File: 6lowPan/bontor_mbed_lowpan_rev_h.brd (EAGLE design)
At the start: 99.6 x 107 mm, 173 parts, among them IC1 SIM900, IC2 74HC595D, IC3 74HC595D, IC4 ADE7758RW, IC5 74HC595D, U2 W5500, X1 NX2520SA

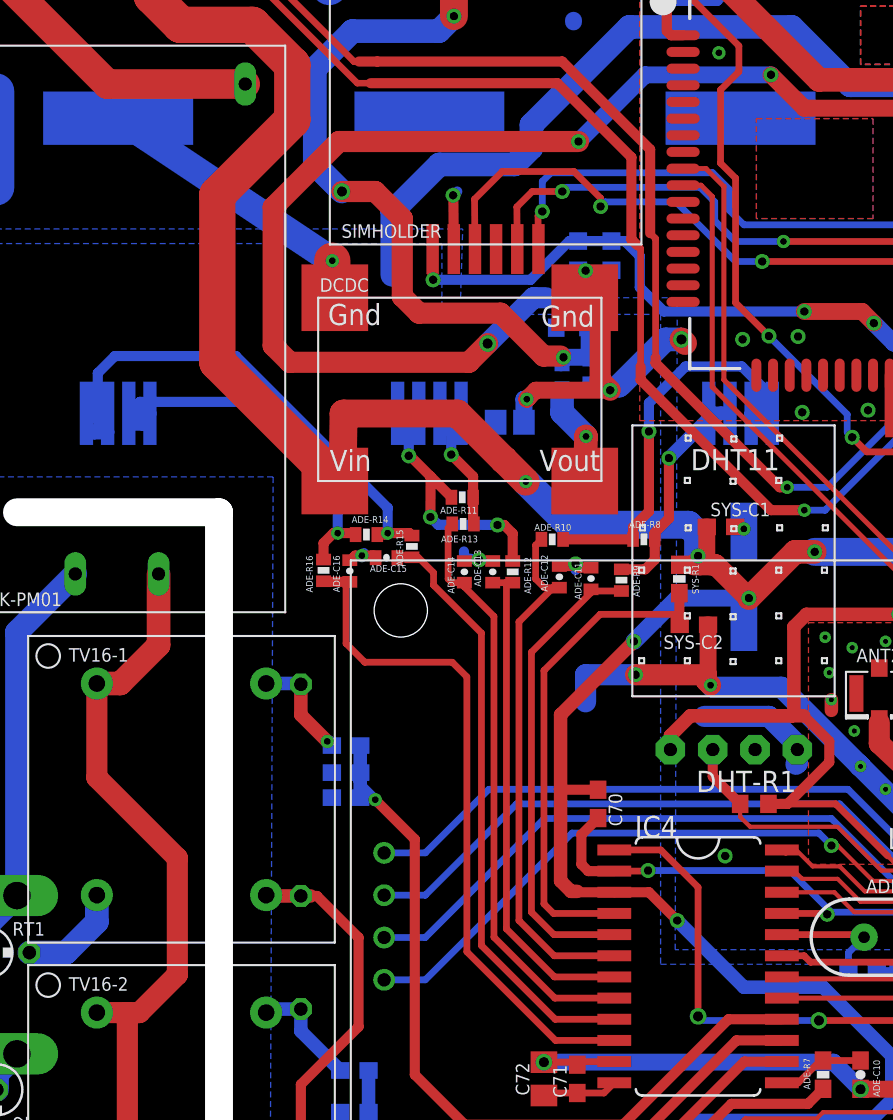
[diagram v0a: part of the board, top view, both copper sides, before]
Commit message: add mcb enhancer BoM and gerber
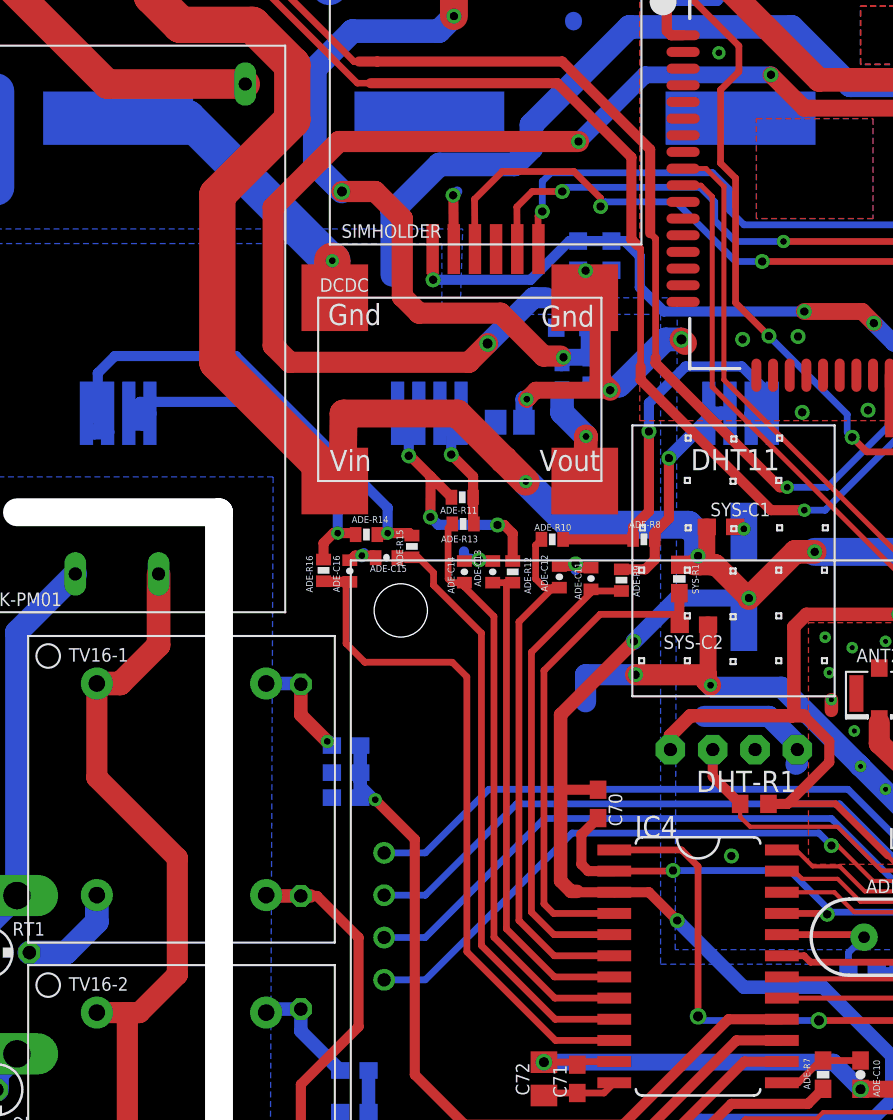
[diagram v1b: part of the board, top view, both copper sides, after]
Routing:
- net DGND: track 380.0 -> 381.0 mm
- net ADE_APCF: track 46.3 -> 47.0 mm
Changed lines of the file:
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@@
 <setting verticaltext="up"/>
 </settings>
-<grid distance="1" unitdist="mm" unit="mm" style="lines" multiple="1" display="yes" altdistance="0.125" altunitdist="mm" altunit="mm"/>
+<grid distance="0.125" unitdist="mm" unit="mm" style="lines" multiple="1" display="yes" altdistance="0.125" altunitdist="mm" altunit="mm"/>
 <layers>
 <layer number="1" name="Top" color="4" fill="1" visible="yes" active="yes"/>
@@
 <wire x1="87.25" y1="36.25" x2="87.25" y2="36.275" width="0.254" layer="1"/>
 <via x="76.25" y="63" extent="1-16" drill="0.6" shape="octagon"/>
-<via x="40.75" y="42.75" extent="1-16" drill="0.5" shape="octagon"/>
-<wire x1="40.75" y1="42.75" x2="49.25" y2="42.75" width="0.4064" layer="16"/>
+<via x="42.25" y="42.75" extent="1-16" drill="0.5" shape="octagon"/>
+<wire x1="42.25" y1="42.75" x2="49.25" y2="42.75" width="0.4064" layer="16"/>
 <wire x1="49.25" y1="42.75" x2="51.75" y2="40.25" width="0.4064" layer="16"/>
 <wire x1="51.75" y1="40.25" x2="55.75" y2="40.25" width="0.4064" layer="16"/>
 <wire x1="55.75" y1="40.25" x2="56.25" y2="39.75" width="0.4064" layer="16"/>
 <wire x1="56.25" y1="39.75" x2="56.25" y2="36.875" width="0.4064" layer="16"/>
-<wire x1="38.7208" y1="42.715" x2="40.715" y2="42.715" width="0.4064" layer="1"/>
-<wire x1="40.715" y1="42.715" x2="40.75" y2="42.75" width="0.4064" layer="1"/>
+<wire x1="38.7208" y1="42.715" x2="42.215" y2="42.715" width="0.4064" layer="1"/>
 <contactref element="SR_OUT1" pad="2"/>
 <contactref element="SR_OUT2" pad="2"/>
@@
 <wire x1="73.7" y1="101.25" x2="72.875" y2="101.3" width="1.4224" layer="1"/>
 <wire x1="72.875" y1="101.3" x2="73" y2="101.375" width="1.4224" layer="1"/>
-<via x="45.375" y="43.625" extent="1-16" drill="0.5"/>
+<via x="45.75" y="43.625" extent="1-16" drill="0.5"/>
 <wire x1="86.25" y1="36.625" x2="86.6" y2="36.275" width="0.254" layer="1"/>
 <wire x1="86.6" y1="36.275" x2="87.25" y2="36.275" width="0.254" layer="1"/>
@@
 <wire x1="10.45" y1="103.45" x2="10.45" y2="105.75" width="0.4064" layer="1"/>
 <wire x1="10.45" y1="105.75" x2="10.4" y2="105.75" width="0.4064" layer="1"/>
-<wire x1="8.95" y1="87.9" x2="21.8" y2="79.345" width="1.6764" layer="16"/>
 <wire x1="19.485" y1="105.75" x2="20.76" y2="104.075" width="1.27" layer="1"/>
 <via x="29.05" y="83.275" extent="1-16" drill="0.5"/>
@@
 <wire x1="10.45" y1="105.75" x2="10.85" y2="106.15" width="1.4" layer="1"/>
 <wire x1="10.85" y1="106.15" x2="11.75" y2="106.15" width="1.4" layer="1"/>
+<wire x1="21.8" y1="79.345" x2="21.655" y2="79.345" width="2.1844" layer="16"/>
+<wire x1="21.655" y1="79.345" x2="13.1" y2="87.9" width="2.1844" layer="16"/>
+<wire x1="13.1" y1="87.9" x2="8.95" y2="87.9" width="2.1844" layer="16"/>
+<wire x1="42.215" y1="42.715" x2="42.25" y2="42.75" width="0.4064" layer="1"/>
 </signal>
 <signal name="VDD">
@@
 <wire x1="48.7942" y1="44" x2="48.7792" y2="43.985" width="0.254" layer="1"/>
 <wire x1="48.8892" y1="43.875" x2="48.7792" y2="43.985" width="0.254" layer="1"/>
-<wire x1="49.0142" y1="43.75" x2="48.7792" y2="43.985" width="0.254" layer="1"/>
 <contactref element="STMF401" pad="56"/>
 <wire x1="50.625" y1="43" x2="52.25" y2="43" width="0.254" layer="1"/>
@@
 <wire x1="70.75" y1="39" x2="73.8798" y2="39" width="0.254" layer="1"/>
 <wire x1="73.8798" y1="39" x2="73.8866" y2="39.0068" width="0.254" layer="1"/>
-<wire x1="38.7208" y1="43.985" x2="41.515" y2="43.985" width="0.4064" layer="1"/>
-<wire x1="41.515" y1="43.985" x2="43.75" y2="41.75" width="0.4064" layer="1"/>
-<wire x1="43.75" y1="41.75" x2="43.75" y2="34" width="0.4064" layer="1"/>
+<wire x1="38.7208" y1="43.985" x2="42.765" y2="43.985" width="0.4064" layer="1"/>
+<wire x1="43.75" y1="43" x2="43.75" y2="34" width="0.4064" layer="1"/>
 <wire x1="43.75" y1="34" x2="43.75" y2="33.75" width="0.4064" layer="16"/>
 <wire x1="43.75" y1="33.75" x2="51" y2="33.75" width="0.4064" layer="16"/>
@@
 <wire x1="69.125" y1="37.375" x2="63.375" y2="37.375" width="0.254" layer="1"/>
 <wire x1="63.375" y1="37.375" x2="59.75" y2="33.75" width="0.254" layer="1"/>
+<wire x1="42.765" y1="43.985" x2="43.75" y2="43" width="0.4064" layer="1"/>
 </signal>
 <signal name="ADE_VARCF">

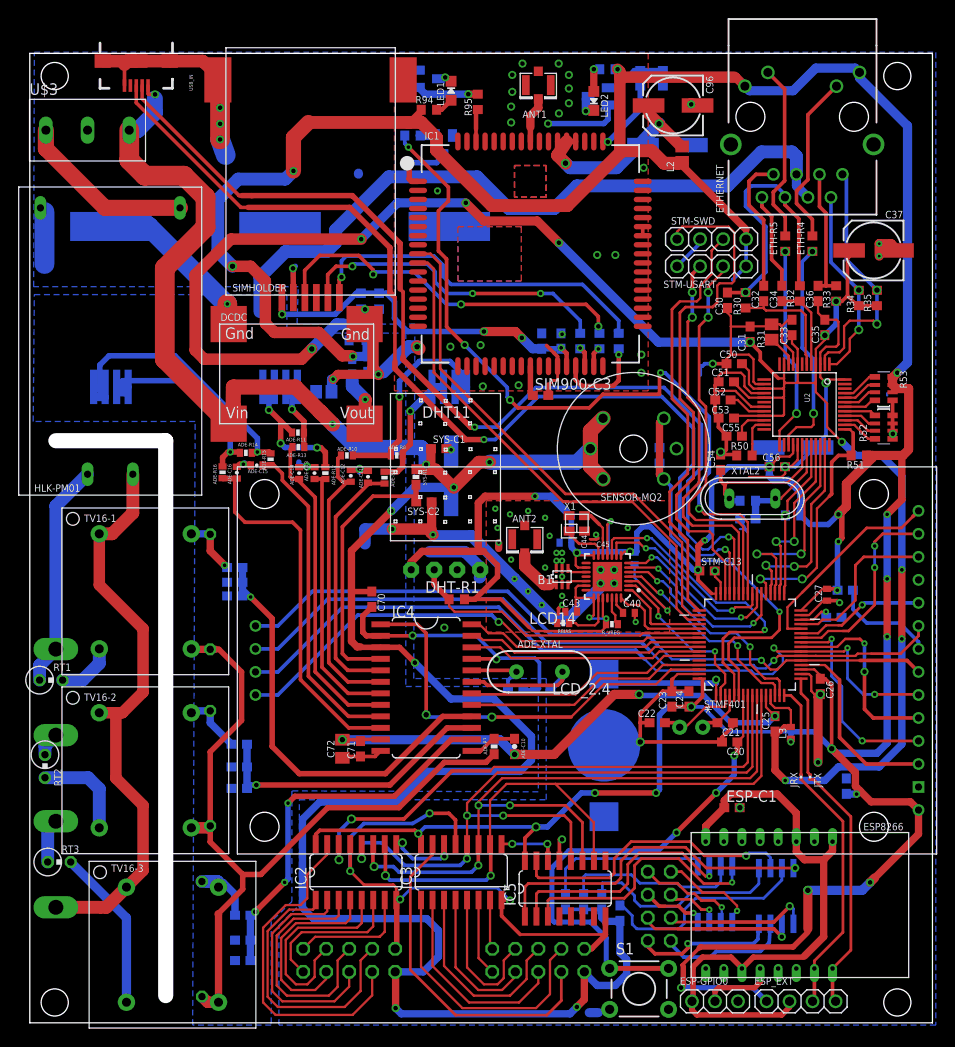
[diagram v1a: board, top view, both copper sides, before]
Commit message: added on off button and remove LCD resstor
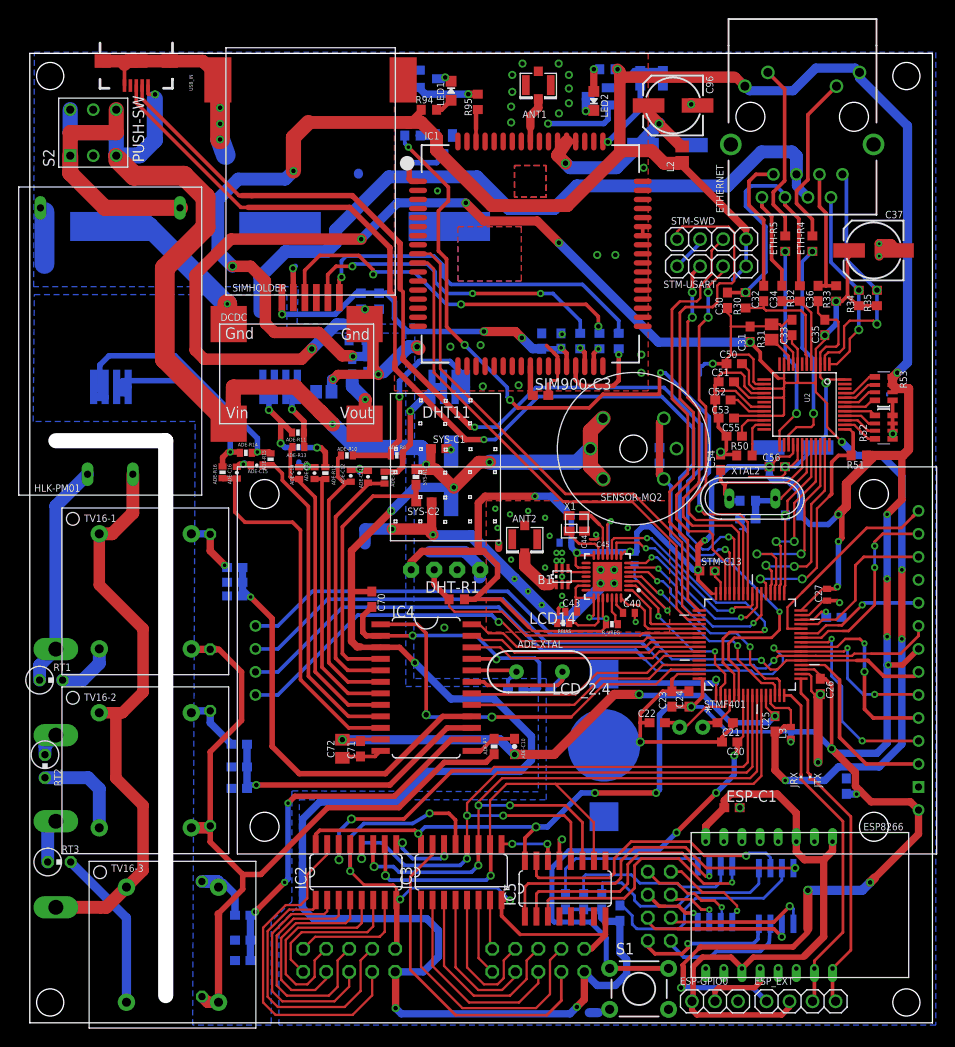
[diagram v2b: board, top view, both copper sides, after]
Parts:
- removed LCD-R1: 680R, SparkFun-Passives:0603-RES
- removed U$3: SW-KN1-102, bontor:KN1-102
- added S2: PUSH-SW, Itead_BP_110825:SWITCH-6PIN-LOCK-2.54MM
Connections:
- removed net LCD_LED: LCD-R1.1, LCD14.LED
- net +5V: now also S2.P$3, S2.P$6; no longer U$3.NO
- net N$79: now also S2.P$1, S2.P$4; no longer U$3.C
- net VDD: now also LCD14.LED; no longer LCD-R1.2
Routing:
- net +5V: track 280.0 -> 293.1 mm
- net LCD_LED: track 11.6 -> 0.00 mm
- net N$79: track 19.6 -> 25.8 mm
- net VDD: track 574.4 -> 578.3 mm, vias 31 -> 32
